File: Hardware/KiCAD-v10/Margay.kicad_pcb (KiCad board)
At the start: 2 copper layers, 50.1 x 30.4 mm, 163 parts, among them J1 SDMMCWR-CRD, J2 CONN_102.54_SCREW, J3 CONN_6SCREW_2.54, J4 USB_C, Q1 DMG3404, Q2 FDN360P, Q3 2N7002, U1 ATMEGA1284M, U10 TLV3691DPF, U11 MIC94090C6, U12 BME280, U13 MAX6070AAUT, U13 MAX6070AAUT18, U14 MCP3421A1, U2 FT231X-Q, U3 TPL5010DDC, U4 SN74LVC1G3157SC70, U5 SN74AUP3G34DCU, U6 TPS797, U6 TPS79733, U7 TPS7A0533DBV, U7 TPS7A05DBV, U8 TPS22916YFP, U9 TPS2104

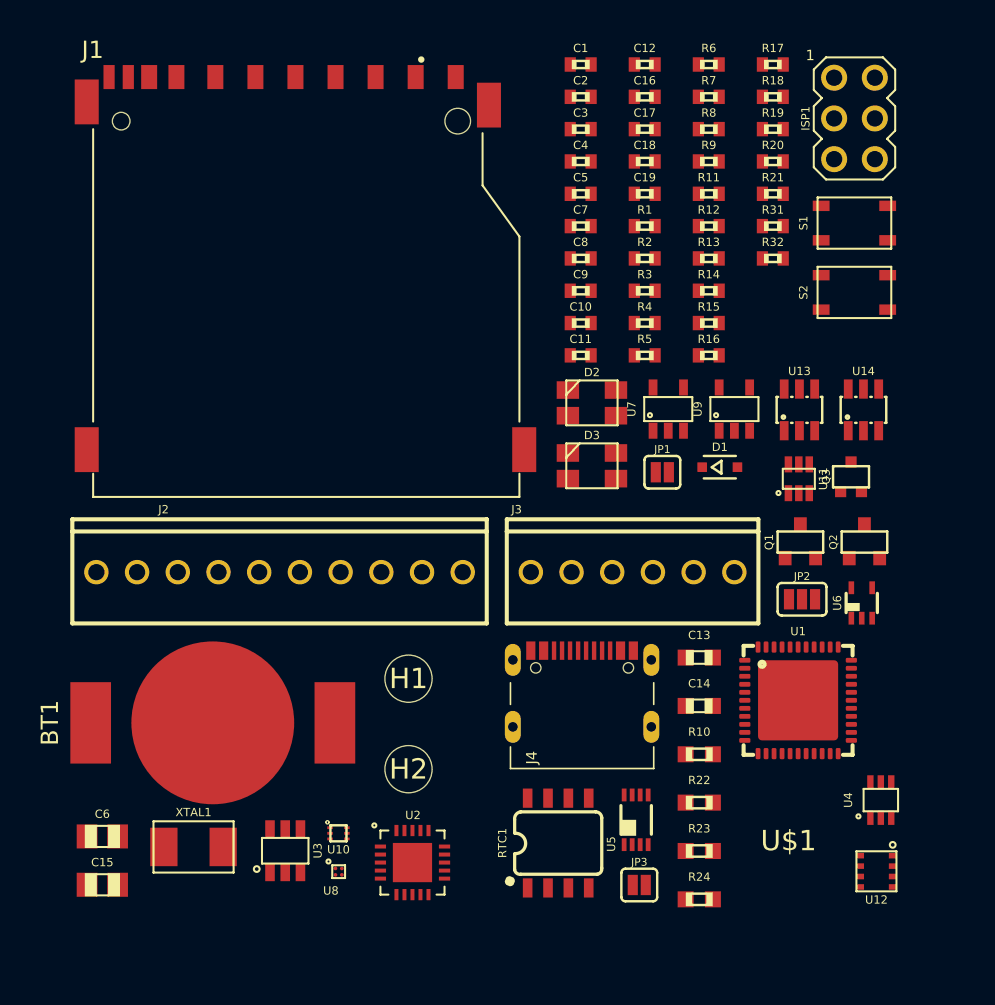
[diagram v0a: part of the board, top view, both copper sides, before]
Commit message: KiCAD-v10 PCB: remove 81 orphaned Margay:-prefixed duplicate footprints
The KiCAD v10 Eagle importer created two footprint instances for every
component: one with a generic name (e.g. R0402) at Eagle coordinates
(125–173 mm), fully connected to the routing, and one with the Margay:
library prefix at a separate coordinate origin (0–50 mm) with no routing
connections. The Margay:-prefixed set is orphaned and unusable.

Removed all 81 Margay:-prefixed footprints. Result: 82 footprints,
1442 track segments, 120 vias — routing fully intact.

Co-Authored-By: Claude Sonnet 4.6 <noreply@anthropic.com>
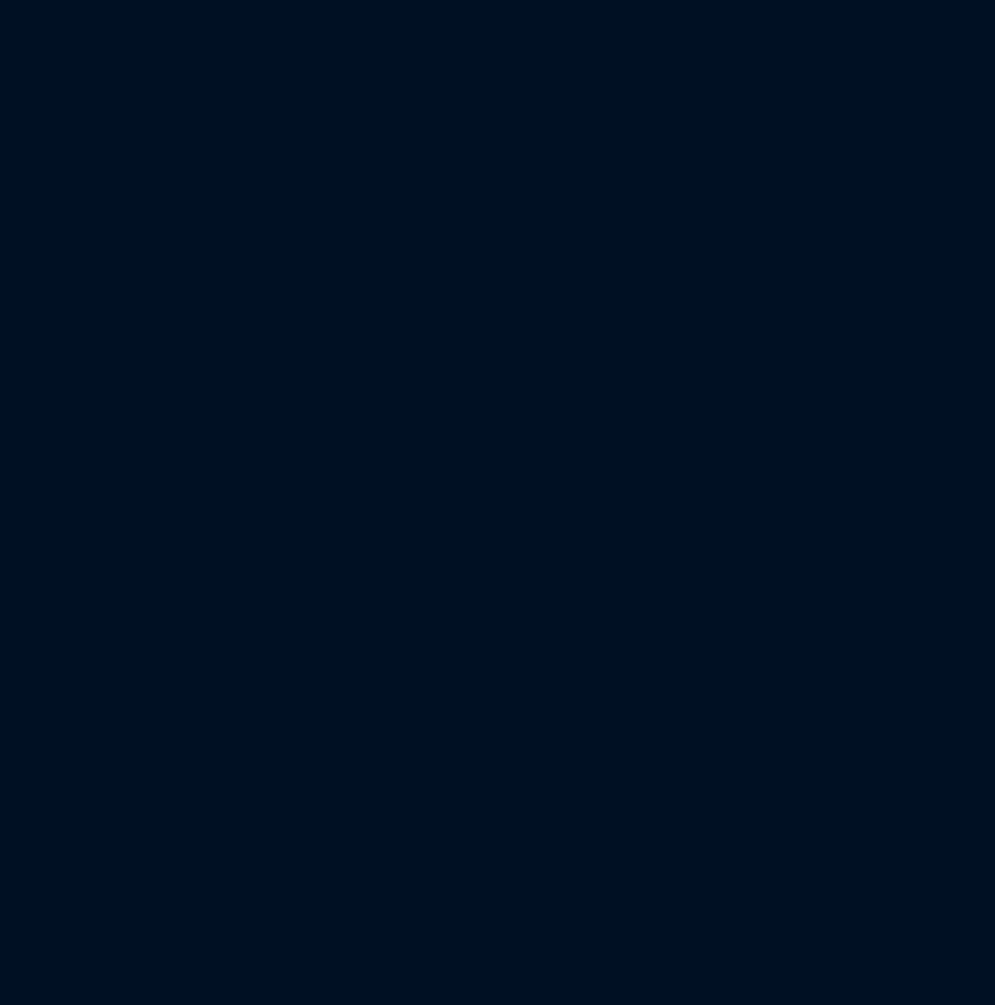
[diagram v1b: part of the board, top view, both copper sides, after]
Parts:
- removed the BT1 at (8.89, 41.6)
- removed the C1 at (31.8, 0.51)
- removed the C10 at (31.8, 16.6)
- removed the C11 at (31.8, 18.7)
- removed the C12 at (35.8, 0.51)
- removed the C13 at (39.2, 37.5)
- removed the C14 at (39.2, 40.5)
- removed the C15 at (2.00, 51.7)
- removed the C16 at (35.8, 2.53)
- removed the C17 at (35.8, 4.54)
- removed the C18 at (35.8, 6.56)
- removed the C19 at (35.8, 8.58)
- removed the C2 at (31.8, 2.53)
- removed the C3 at (31.8, 4.54)
- removed the C4 at (31.8, 6.56)
- removed the C5 at (31.8, 8.58)
- removed the C6 at (2.00, 48.7)
- removed the C7 at (31.8, 10.6)
- removed the C8 at (31.8, 12.6)
- removed the C9 at (31.8, 14.6)
- removed the D1 at (40.5, 25.6)
- removed the D2 at (32.5, 21.6)
- removed the D3 at (32.5, 25.6)
- removed the H1 at (21.1, 38.8)
- removed the H2 at (21.1, 44.5)
- removed the ISP1 at (48.9, 3.87)
- removed the J1 at (14.7, 2.04)
- removed the J2 at (13.1, 32.2)
- removed the J3 at (35.1, 32.2)
- removed the J4 at (31.9, 44.4)
- removed the JP1 at (36.9, 26.0)
- removed the JP2 at (45.7, 33.9)
- removed the JP3 at (35.5, 51.7)
- removed the Q1 at (45.6, 30.3)
- removed the Q2 at (49.6, 30.3)
- removed the Q3 at (48.7, 26.2)
- removed the R1 at (35.8, 10.6)
- removed the R10 at (39.2, 43.6)
- removed the R11 at (39.8, 8.58)
- removed the R12 at (39.8, 10.6)
- removed the R13 at (39.8, 12.6)
- removed the R14 at (39.8, 14.6)
- removed the R15 at (39.8, 16.6)
- removed the R16 at (39.8, 18.7)
- removed the R17 at (43.8, 0.51)
- removed the R18 at (43.8, 2.53)
- removed the R19 at (43.8, 4.54)
- removed the R2 at (35.8, 12.6)
- removed the R20 at (43.8, 6.56)
- removed the R21 at (43.8, 8.58)
- removed the R22 at (39.2, 46.6)
- removed the R23 at (39.2, 49.6)
- removed the R24 at (39.2, 52.6)
- removed the R3 at (35.8, 14.6)
- removed the R31 at (43.8, 10.6)
- removed the R32 at (43.8, 12.6)
- removed the R4 at (35.8, 16.6)
- removed the R5 at (35.8, 18.7)
- removed the R6 at (39.8, 0.51)
- removed the R7 at (39.8, 2.53)
- removed the R8 at (39.8, 4.54)
- removed the R9 at (39.8, 6.56)
- removed the RTC1 at (30.4, 49.1)
- removed the S1 at (48.9, 10.4)
- removed the S2 at (48.9, 14.7)
- removed the U$1 at (44.8, 49.0)
- removed the U1 at (45.4, 40.2)
- removed the U10 at (16.7, 48.5)
- removed the U11 at (45.5, 26.4)
- removed the U12 at (50.3, 50.9)
- removed the U13 at (45.5, 22.1)
- removed the U14 at (49.5, 22.1)
- removed the U2 at (21.4, 50.3)
- removed the U3 at (13.4, 49.6)
- removed the U4 at (50.6, 46.4)
- removed the U5 at (35.3, 47.6)
- removed the U6 at (49.4, 34.1)
- removed the U7 at (37.3, 22.0)
- removed the U8 at (16.7, 50.9)
- removed the U9 at (41.4, 22.0)
- removed the XTAL1 at (7.69, 49.3)
